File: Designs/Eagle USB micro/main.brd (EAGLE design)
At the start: 17.3 x 25.4 mm, 6 parts

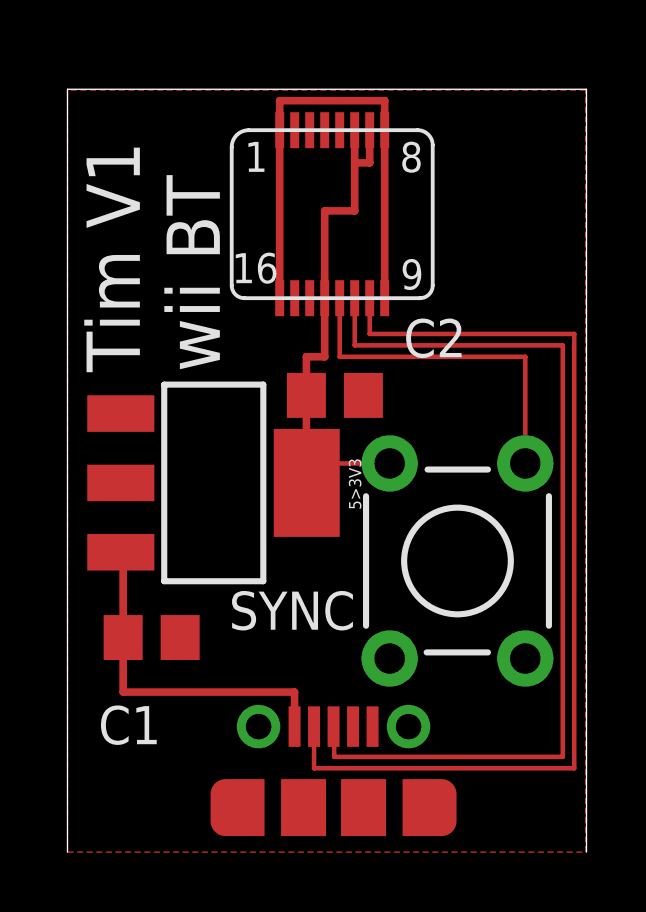
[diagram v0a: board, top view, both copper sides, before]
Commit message: Fixed dimensions plane missing line
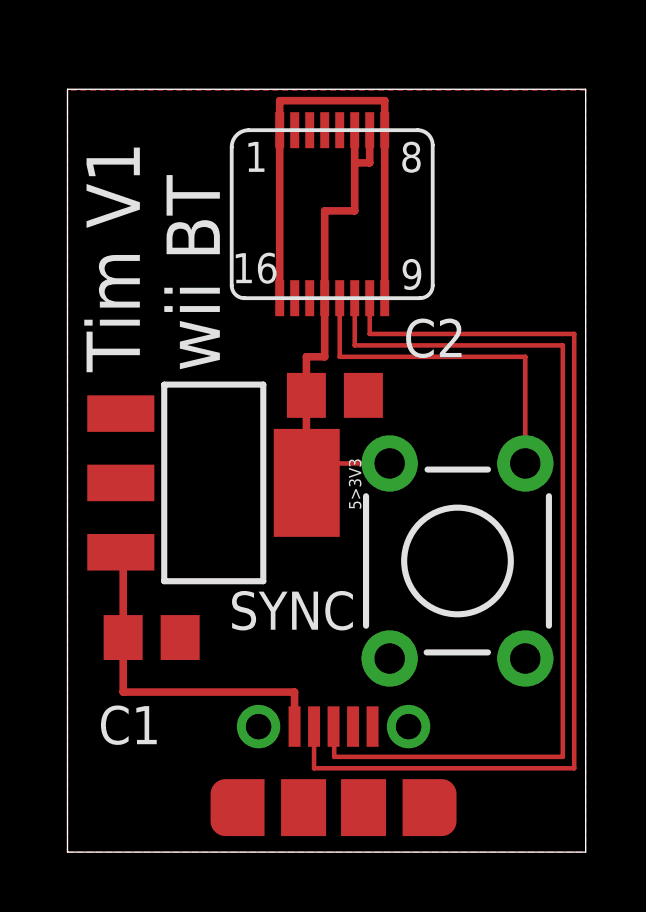
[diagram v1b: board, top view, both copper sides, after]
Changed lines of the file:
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@@
 <board>
 <plain>
-<wire x1="17.3" y1="0" x2="17.3" y2="25.428" width="0" layer="20"/>
-<wire x1="17.3" y1="25.428" x2="0" y2="25.428" width="0" layer="20"/>
+<wire x1="17.272" y1="0" x2="17.272" y2="25.428" width="0" layer="20"/>
+<wire x1="17.272" y1="25.428" x2="0" y2="25.428" width="0" layer="20"/>
 <wire x1="0" y1="25.428" x2="0" y2="0" width="0" layer="20"/>
 <text x="5.08" y="16.002" size="1.778" layer="21" font="vector" rot="R90">Tim V1
 wii BT</text>
+<wire x1="0" y1="0" x2="17.272" y2="0" width="0" layer="20"/>
 </plain>
 <attributes>
